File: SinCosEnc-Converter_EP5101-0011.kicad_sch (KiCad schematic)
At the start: 11 parts, among them J1 Conn_01x05_Pin, U2 AM26LS31CDR, X2 D-SUB-DR-15PCG-AB

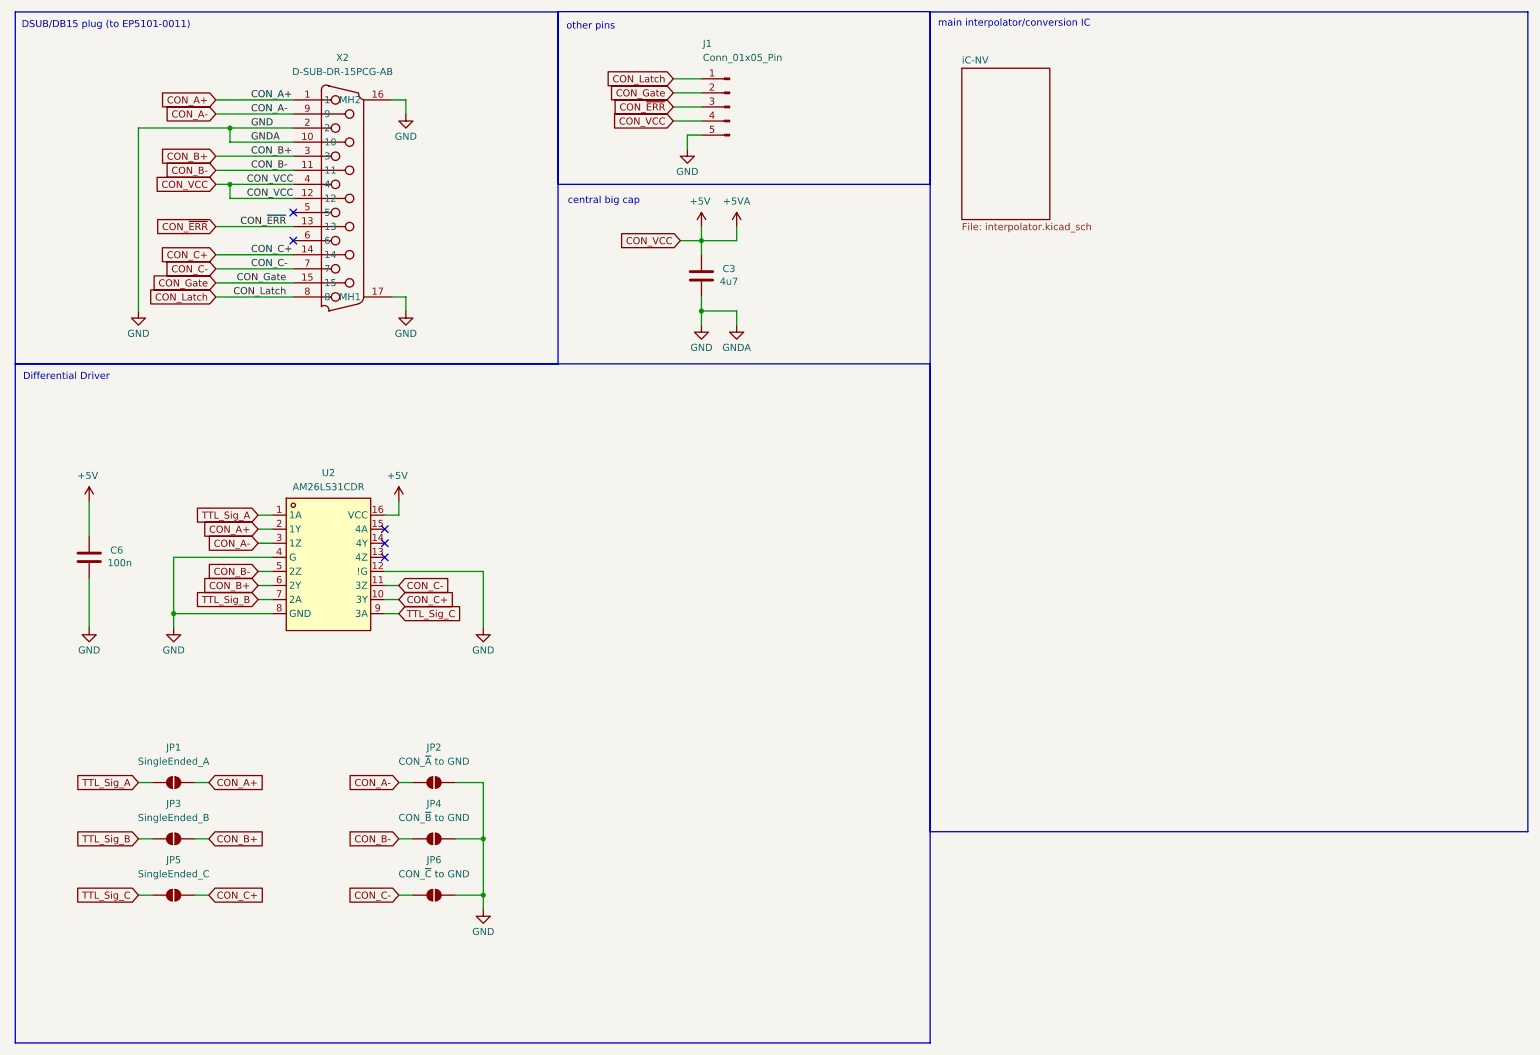
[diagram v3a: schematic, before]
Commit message: further ESD protection, PCB layout started
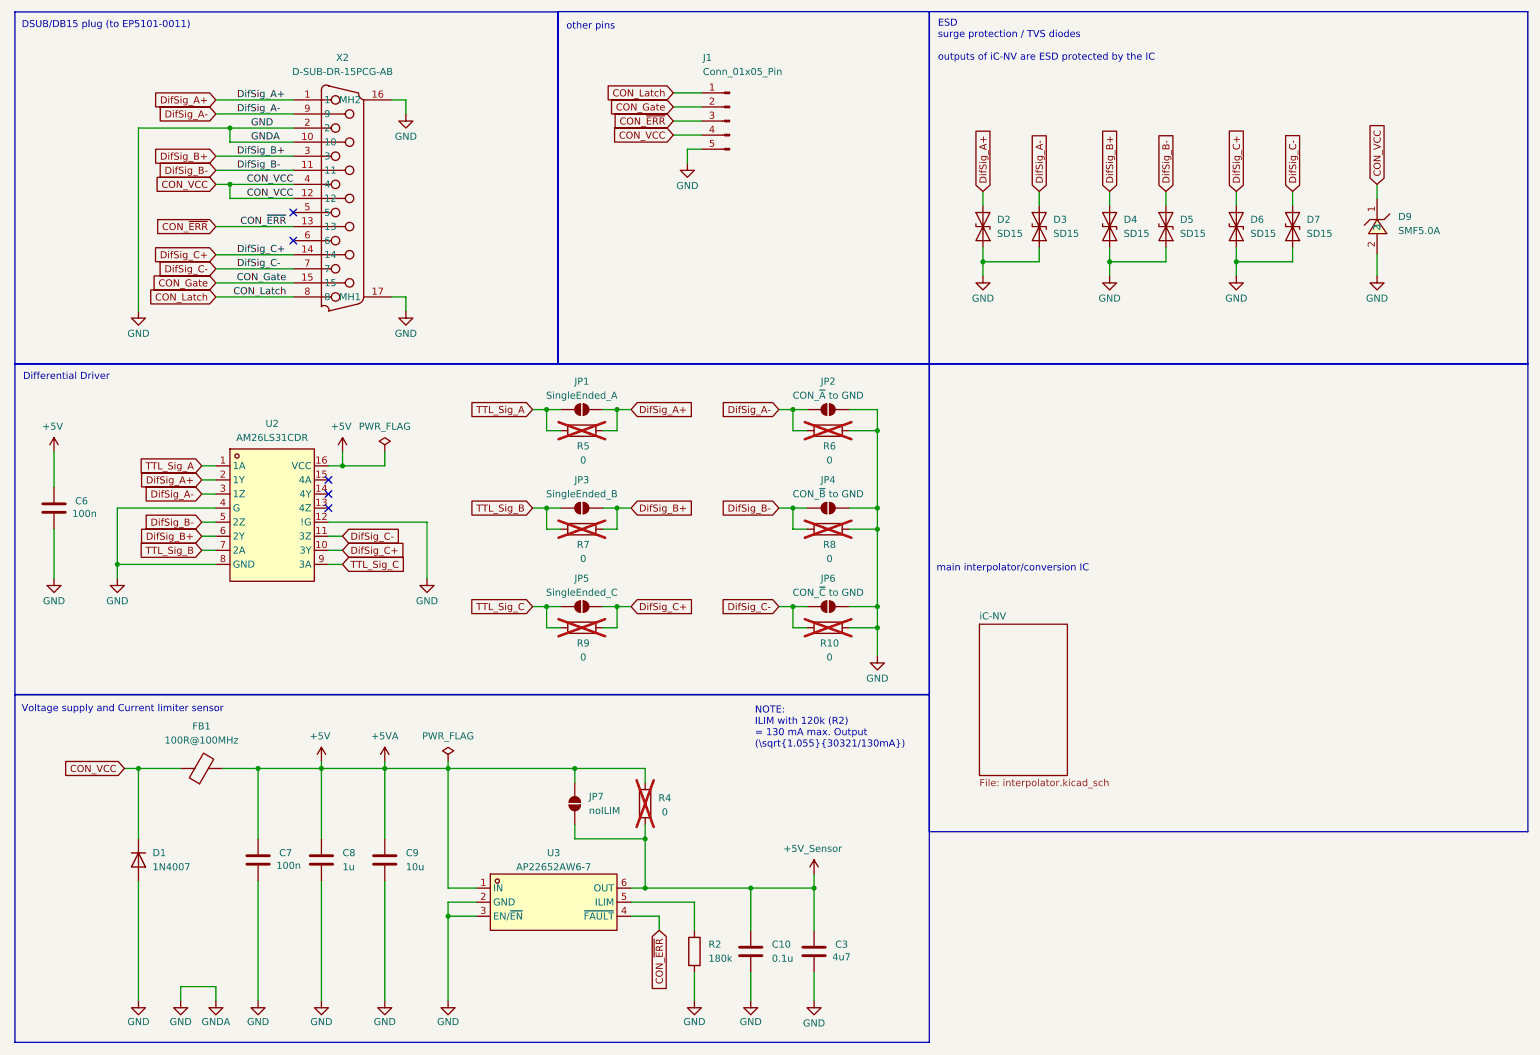
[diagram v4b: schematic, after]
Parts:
- added C10: 0.1u, Capacitor_SMD:C_0603_1608Metric, symbol Device:C
- added C7: 100n, Capacitor_SMD:C_0603_1608Metric, symbol Device:C
- added C8: 1u, Capacitor_SMD:C_0603_1608Metric, symbol Device:C
- added C9: 10u, Capacitor_SMD:C_0603_1608Metric, symbol Device:C
- added D1: 1N4007, Diode_SMD:D_SMA, symbol Diode:1N4007
- added D2, D3, D4, D5, D6, D7: SD15, Diode_SMD:D_SOD-323, symbol Diode:SD15_SOD323
- added D9: SMF5.0A, easyeda2kicad:SOD-123F_L2.8-W1.8-LS3.7-RD, symbol easyeda2kicad:SMF5.0A_C151296
- added FB1: 100R@100MHz, easyeda2kicad:L0603, symbol Device:FerriteBead
- added JP7: noILIM, Jumper:SolderJumper-2_P1.3mm_Open_RoundedPad1.0x1.5mm, symbol Jumper:SolderJumper_2_Open
- added R10, R4, R5, R6, R7, R8, R9: 0, Resistor_SMD:R_0603_1608Metric, symbol Device:R
- added R2: 180k, Resistor_SMD:R_0603_1608Metric, symbol Device:R
- added U3: AP22652AW6-7, easyeda2kicad:SOT-23-6_L2.9-W1.6-P0.95-LS2.8-BL, symbol project_library:AP22652AW6-7
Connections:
- net +5V: now also C7.2, C8.2, C9.2, FB1.2, JP7.2 (B), R4.2, U3.1 (IN); no longer C3.2, J1.4 (Pin_4), X2.12, X2.4
- net CON_~{ERR}: now also U3.4 (~{FAULT})
- net GND: now also C10.1, C7.1, C8.1, C9.1, D1.2 (A), D2.1 (A1), D3.1 (A1), D4.1 (A1), D5.1 (A1), D6.1 (A1), D7.1 (A1), D9.2, R10.1, R2.2, R6.1, R8.1, U3.2 (GND), U3.3 (EN/~{EN})
- net TTL_Sig_A: now also R5.2
- net TTL_Sig_B: now also R7.2
- net TTL_Sig_C: now also R9.2
- net CON_A+ renamed DifSig_A+
- net DifSig_A+: now also D2.2 (A2), R5.1
- net CON_A- renamed DifSig_A-
- net DifSig_A-: now also D3.2 (A2), R6.2
- net CON_B+ renamed DifSig_B+
- net DifSig_B+: now also D4.2 (A2), R7.1
- net CON_B- renamed DifSig_B-
- net DifSig_B-: now also D5.2 (A2), R8.2
- net CON_C+ renamed DifSig_C+
- net DifSig_C+: now also D6.2 (A2), R9.1
- net CON_C- renamed DifSig_C-
- net DifSig_C-: now also D7.2 (A2), R10.2
- new net: R2.1, U3.5 (ILIM)
- new net +5V_Sensor: C10.2, C3.2, JP7.1 (A), R4.1, U3.6 (OUT)
- new net CON_VCC: D1.1 (K), D9.1, FB1.1, J1.4 (Pin_4), X2.12, X2.4
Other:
- note added: "ESD surge protection / TVS diodes outputs of iC-NV are ESD protected by the IC"
- note added: "NOTE: ILIM with 120k (R2) = 130 mA max. Output (\sqrt{1.055}{30321/130mA})"
- note added: "Voltage supply and Current limiter sensor"
- note removed: "central big cap"
- title: Header and Outputs -> Header, Outputs and ESD
- moved on the sheet: C3, C6, J1, JP1, JP2, JP3, JP4, JP5, JP6, U2

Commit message: v0.9.2 finished, board routed
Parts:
- removed D1: 1N4007, Diode_SMD:D_SMA, symbol Diode:1N4007
- added JP8: DiagRPP, Jumper:SolderJumper-3_P1.3mm_Bridged12_RoundedPad1.0x1.5mm, symbol Jumper:SolderJumper_3_Bridged12
- added U4: LM66100DCKR, easyeda2kicad:SC-70-6_L2.0-W1.3-P0.65-LS2.1-BL, symbol easyeda2kicad:LM66100DCKR
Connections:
- net CON_VCC: now also U4.1 (VIN); no longer FB1.1
- net CON_~{ERR}: now also JP8.3 (B)
- net GND: now also JP8.2 (C), U4.2 (GND), U4.3 (~{CE}), U4.4 (NC)
- new net: FB1.1, U4.6 (VOUT)
- new net: JP8.1 (A), U4.5 (ST)
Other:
- moved on the sheet: C10, C3, C7, C8, C9, FB1, JP7, R2, R4, U3

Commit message: first theoretical working PCB finished (v0.9.3)
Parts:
- renumbered R2 to R1, R4 to R2
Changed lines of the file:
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@@
 		(dnp no)
 		(fields_autoplaced yes)
-		(property "Reference" "R2"
+		(property "Reference" "R1"
 			(at 149.86 181.6099 0)
 			(effects
@@
 			(project "SinCosEnc-Converter_EP5101-0011"
 				(path "/65c0920c-b33d-485e-a4e4-15145e9bcf4b"
-					(reference "R2")
+					(reference "R1")
 					(unit 1)
 				)
@@
 		(on_board yes)
 		(dnp yes)
-		(property "Reference" "R4"
+		(property "Reference" "R2"
 			(at 141.986 156.464 0)
 			(effects
@@
 			(project "SinCosEnc-Converter_EP5101-0011"
 				(path "/65c0920c-b33d-485e-a4e4-15145e9bcf4b"
-					(reference "R4")
+					(reference "R2")
 					(unit 1)
 				)

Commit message: version 0.9.6 finished
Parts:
- removed D9: SMF5.0A, easyeda2kicad:SOD-123F_L2.8-W1.8-LS3.7-RD, symbol easyeda2kicad:SMF5.0A_C151296
- removed J1: Conn_01x05_Pin, Connector_JST:JST_XH_B5B-XH-A_1x05_P2.50mm_Vertical, symbol Connector:Conn_01x05_Pin
- removed JP8: DiagRPP, Jumper:SolderJumper-3_P1.3mm_Bridged12_RoundedPad1.0x1.5mm, symbol Jumper:SolderJumper_3_Bridged12
- added C10, C12: 47u, Capacitor_SMD:C_1206_3216Metric, symbol Device:C
- added C13: 4n7, Capacitor_SMD:C_1808_4520Metric, symbol Device:C
- added D1: SMAJ5.0CA, Diode_SMD:D_SMA, symbol Diode:SMAJ5.0CA
- added D10, D11, D12: ESD401DPYR, CostumLibrary:Texas_DPY0002A_0.6x1mm_P0.65mm, symbol Diode:SMAJ5.0CA
- added R12: 1M, Resistor_SMD:R_2010_5025Metric, symbol Device:R
- R1: value 180k -> 215k; LCSC Part (none) -> C22954
- renumbered C10 to C11
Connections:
- net +5V: now also FB1.1, C10.2; no longer FB1.2
- net +5V_Sensor: now also C12.2
- net CON_VCC: now also D1.2 (A2)
- net CON_~{ERR}: now also U4.5 (ST)
- net GND: now also C10.1, C12.1, C13.2, D1.1 (A1), D10.1 (A1), D11.1 (A1), D12.1 (A1), R12.2; no longer X2.16 (MH2), X2.17 (MH1)
- net TTL_Sig_A: now also D10.2 (A2)
- net TTL_Sig_B: now also D11.2 (A2)
- net TTL_Sig_C: now also D12.2 (A2)
- net at U4.6 (VOUT): now also FB1.2; no longer FB1.1
- net CON_Gate: no longer names the net of X2.15
- net CON_Latch: no longer names the net of X2.8
- new net GNDS: C13.1, R12.1, X2.16 (MH2), X2.17 (MH1)
- no-connect marks 5 -> 7
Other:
- note added: "ESD surge protection / TVS diodes and Shielding inputs of iC-NV are ESD protected by the IC and its analog frontend"
- note added: "NOTE: ILIM with 215k (R1) = 105 mA max. Output (\sqrt{1.055}{30321/105mA})"
- note removed: "ESD surge protection / TVS diodes outputs of iC-NV are ESD protected by the IC"
- note removed: "NOTE: ILIM with 120k (R2) = 130 mA max. Output (\sqrt{1.055}{30321/130mA})"
- note removed: "other pins"
- moved on the sheet: C11, C3, C7, C8, C9, D2, D3, D4, D5, D6, D7, FB1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
